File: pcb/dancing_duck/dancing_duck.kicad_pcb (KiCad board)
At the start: 2 copper layers, 60.2 x 53.6 mm, 12 parts, among them J1 Conn_01x02, J2 Conn_01x02, J3 Conn_01x02, J4 Conn_01x02, J5 Conn_01x02_Pin, J6 Conn_01x01_Pin

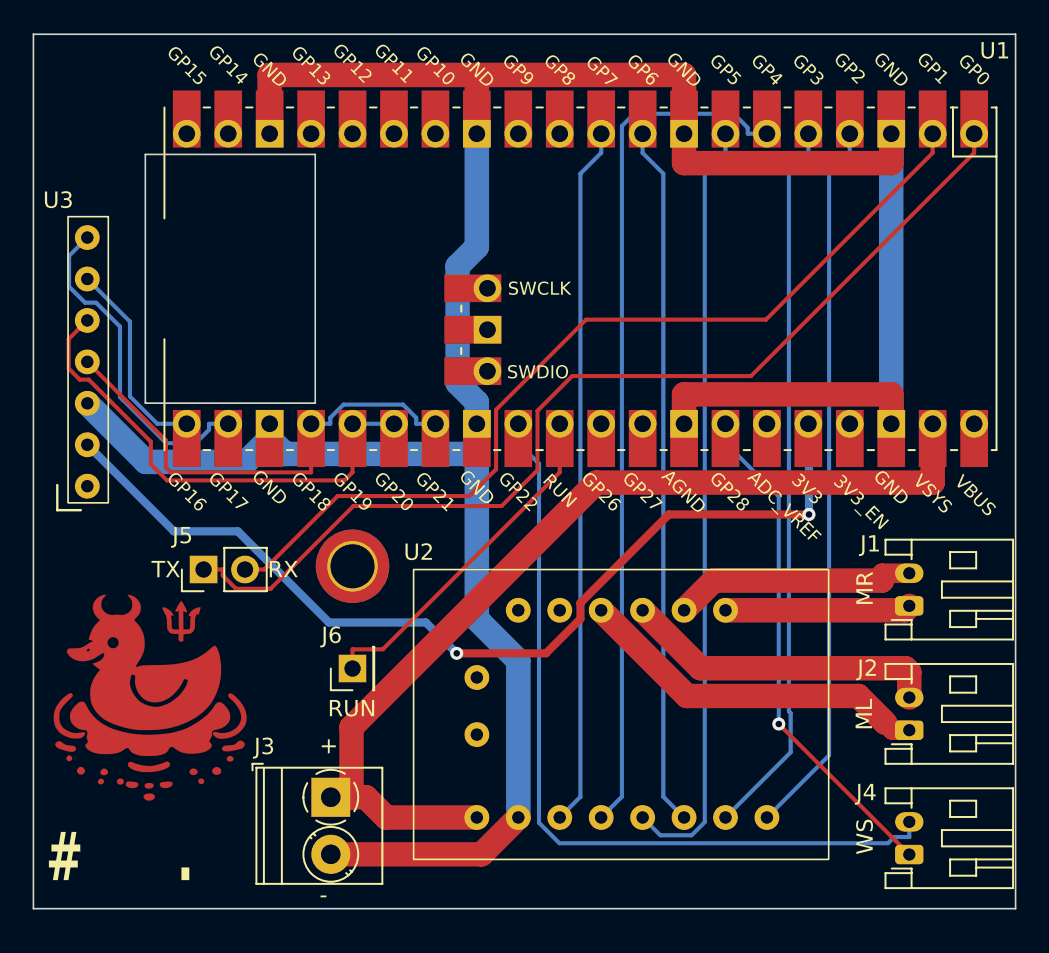
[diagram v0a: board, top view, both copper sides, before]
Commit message: feat: add battery adc to pcb
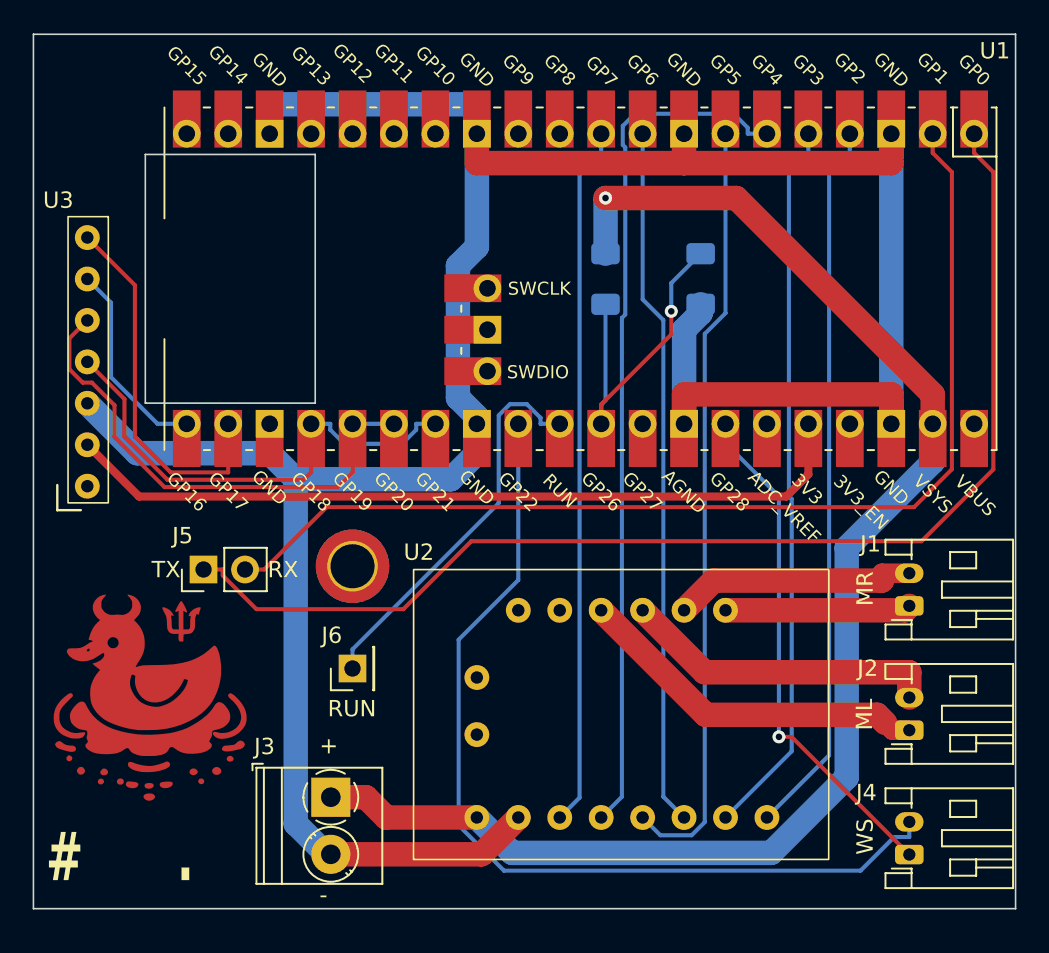
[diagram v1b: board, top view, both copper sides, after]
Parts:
- added R1: 220k, Resistor_SMD:R_1206_3216Metric_Pad1.30x1.75mm_HandSolder, B.Cu at (159.3, 85.3)
- added R2: 330k, Resistor_SMD:R_1206_3216Metric_Pad1.30x1.75mm_HandSolder, B.Cu at (165.1, 85.3)
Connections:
- U1 pad 31: unconnected-(U1-GP26-Pad31) -> Net-(U1-GP26)
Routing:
- net VCC: track 59.2 -> 89.1 mm, vias 0 -> 1
- net Net-(U1-GP26): track 0.00 -> 20.4 mm, vias 0 -> 1
- net Net-(J5-Pin_1): track 62.3 -> 74.2 mm
- net Net-(J5-Pin_2): track 56.0 -> 66.9 mm
- net +3V3: track 59.2 -> 49.2 mm, vias 2 -> 0
- net Net-(J4-Pin_2): track 49.3 -> 56.7 mm
- net GND: track 170.2 -> 174.2 mm
- net Net-(J6-Pin_1): track 21.3 -> 24.0 mm
- net Net-(U1-GP17): track 20.4 -> 23.0 mm
- net Net-(U1-GP18): track 29.5 -> 30.3 mm
- net Net-(U1-GP19): track 30.2 -> 30.8 mm

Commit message: fix: update pcb to beta
- Fix daughter board pin hole size
- Add better support for connecting J-Link
- Update silkscreen
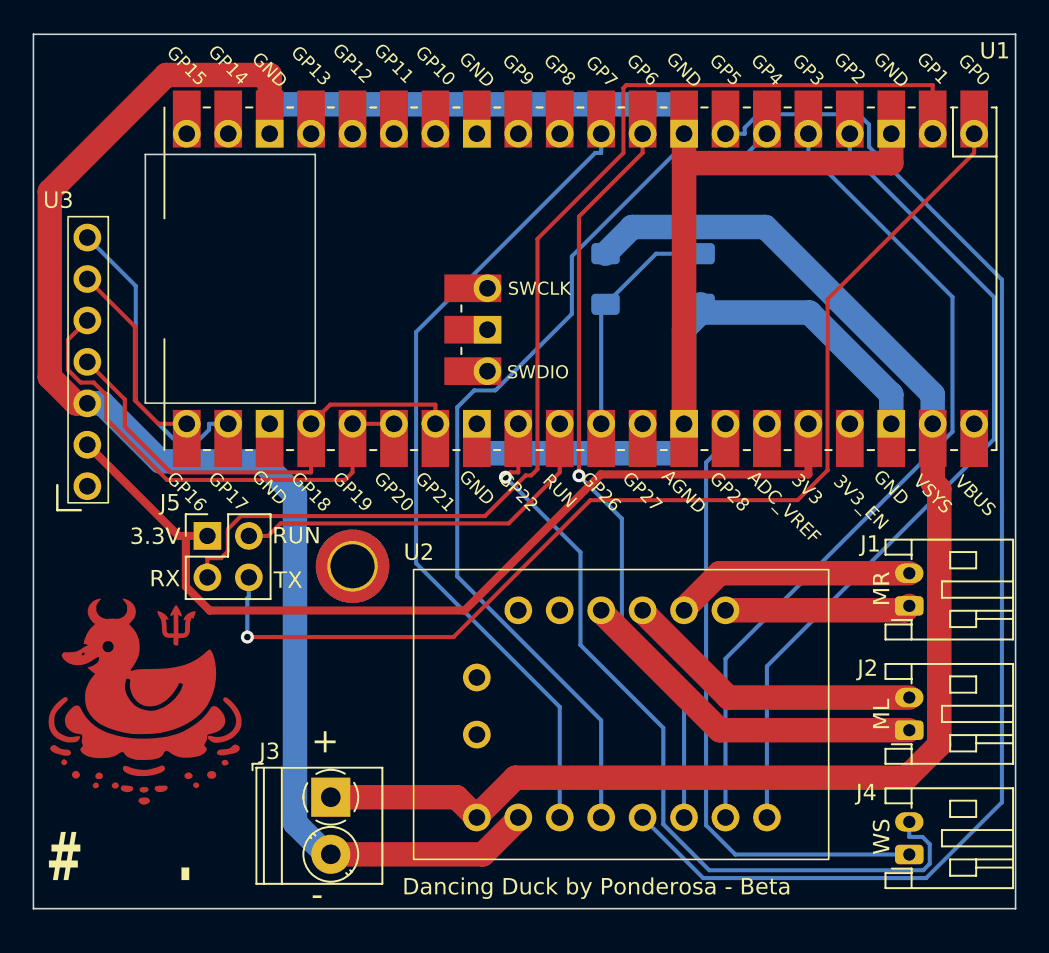
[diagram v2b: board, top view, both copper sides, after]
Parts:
- removed J6: Conn_01x01_Pin, Connector_PinHeader_2.54mm:PinHeader_1x01_P2.54mm_Vertical
- J5: value Conn_01x02_Pin -> Conn_02x02_Counter_Clockwise; footprint Connector_PinHeader_2.54mm:PinHeader_1x02_P2.54mm_Vertical -> Connector_PinHeader_2.54mm:PinHeader_2x02_P2.54mm_Vertical
- moved J5 2.07 mm to (134.9, 101.1), turned to 0 degrees
- moved G*** 0.39 mm to (131.1, 111.3)
- moved G_LOGO 0.39 mm to (131.1, 111.3)
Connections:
- J5 pad 1: Net-(J5-Pin_1) -> +3V3
- U1 pad 1: Net-(J5-Pin_1) -> Net-(J5-Pin_4)
- U1 pad 2: Net-(J5-Pin_2) -> Net-(J5-Pin_3)
- U1 pad 30: Net-(J6-Pin_1) -> Net-(J5-Pin_2)
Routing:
- net Net-(J5-Pin_1): track 74.2 -> 0.00 mm
- net Net-(J5-Pin_3): track 0.00 -> 72.0 mm
- net Net-(J5-Pin_4): track 0.00 -> 67.8 mm, vias 0 -> 1
- net Net-(J5-Pin_2): track 66.9 -> 23.6 mm
- net Net-(U1-GP5): track 47.3 -> 80.2 mm
- net Net-(J6-Pin_1): track 24.0 -> 0.00 mm
- net GND: track 174.2 -> 190.2 mm
- net +3V3: track 49.2 -> 58.1 mm
- net Net-(U1-GP7): track 43.0 -> 50.5 mm
- net Net-(U1-GP2): track 44.0 -> 51.3 mm
- net Net-(U1-GP3): track 44.2 -> 51.3 mm
- net Net-(J4-Pin_1): track 31.5 -> 38.3 mm, vias 1 -> 0
- net Net-(J4-Pin_2): track 56.7 -> 50.4 mm, vias 0 -> 1
- net Net-(U1-GP26): track 20.4 -> 14.6 mm, vias 1 -> 0
- net Net-(U1-GP17): track 23.0 -> 18.7 mm
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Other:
- board text added: "3.3V"
- board text added: "Dancing Duck by Ponderosa - Beta"
- board text added: "https://github.com/Ponderosa/dancing_duck"

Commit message: fix: add capacitor to pcb
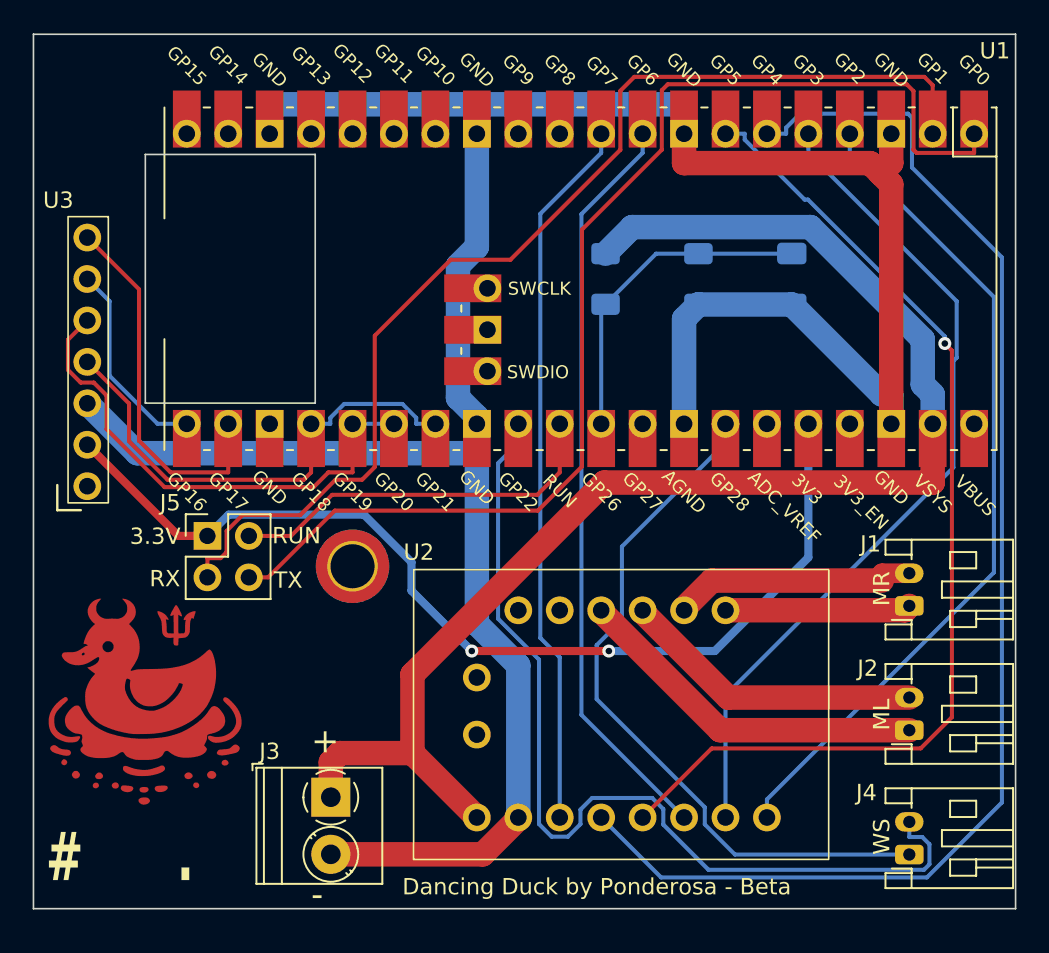
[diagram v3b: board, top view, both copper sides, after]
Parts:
- added C1: 1000pf, Capacitor_SMD:C_1206_3216Metric_Pad1.33x1.80mm_HandSolder, B.Cu at (170.7, 85.3)
- moved R2 0.14 mm to (165.0, 85.3)
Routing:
- net Net-(U1-GP4): track 56.8 -> 82.0 mm
- net GND: track 190.2 -> 170.2 mm
- net Net-(U1-GP5): track 80.2 -> 63.8 mm, vias 0 -> 1
- net Net-(J4-Pin_2): track 50.4 -> 57.9 mm, vias 1 -> 0
- net Net-(U1-GP7): track 50.5 -> 43.9 mm
- net Net-(U1-GP26): track 14.6 -> 20.1 mm
- net Net-(J4-Pin_1): track 38.3 -> 43.9 mm
- net Net-(J5-Pin_4): track 67.8 -> 72.6 mm, vias 1 -> 0
- net Net-(U1-GP17): track 18.7 -> 23.0 mm
- net +3V3: track 58.1 -> 62.1 mm, vias 0 -> 2
- net Net-(J5-Pin_3): track 72.0 -> 68.6 mm
- net Net-(U1-GP19): track 30.3 -> 31.0 mm
- net Net-(U1-GP18): track 29.8 -> 30.3 mm
- net Net-(U1-GP6): track 46.2 -> 46.1 mm, vias 1 -> 0

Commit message: feat: add RX to GND solder bridge to PCB
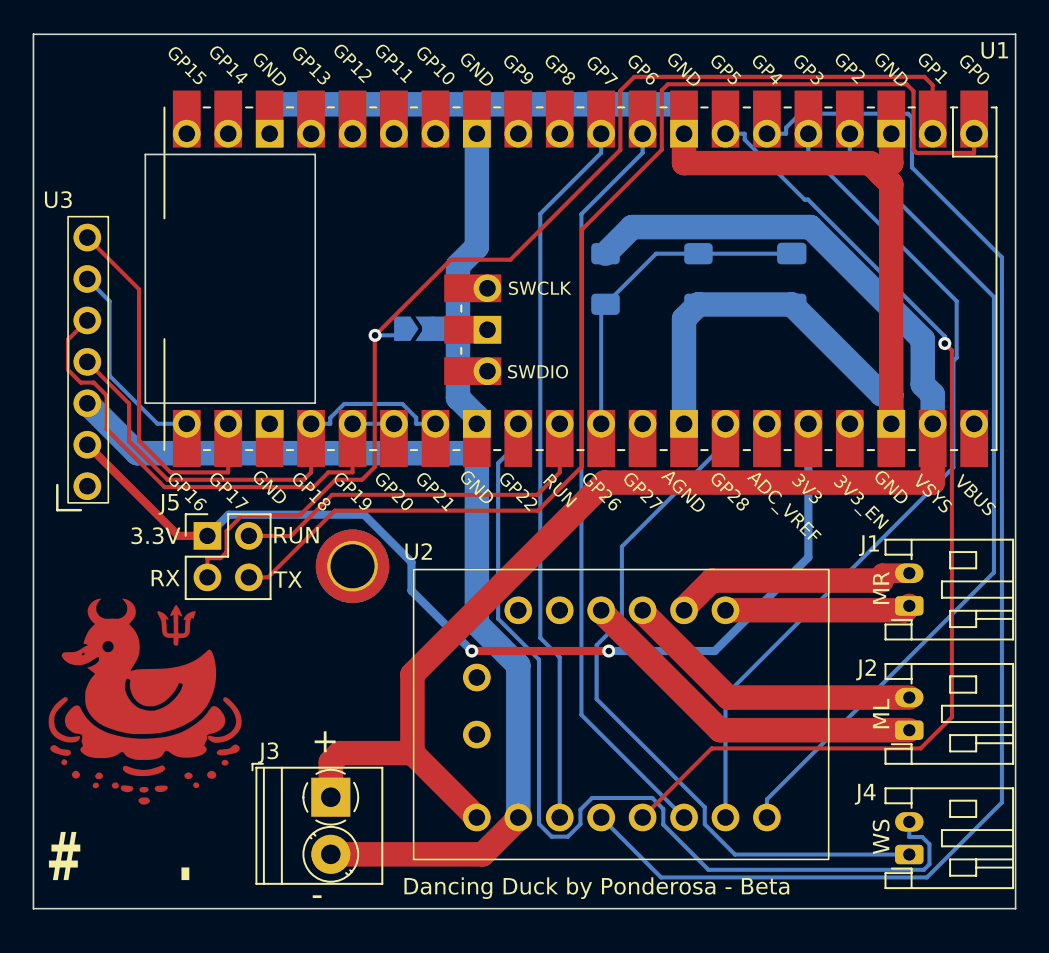
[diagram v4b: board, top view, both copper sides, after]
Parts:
- added R3: 0 DNP, Jumper:SolderJumper-2_P1.3mm_Open_TrianglePad1.0x1.5mm, B.Cu at (147.5, 88.4)
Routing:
- net Net-(J5-Pin_3): track 68.6 -> 70.5 mm, vias 0 -> 1
- net GND: track 170.2 -> 171.6 mm
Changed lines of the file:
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@@
     )
+  )
+  (footprint "Jumper:SolderJumper-2_P1.3mm_Open_TrianglePad1.0x1.5mm" (layer "B.Cu")
+    (at 147.537 88.392)
+    (descr "SMD Solder Jumper, 1x1.5mm Triangular Pads, 0.3mm gap, open")
+    (tags "solder jumper open")
+    (property "Sheetfile" "dancing_duck.kicad_sch")
+    (property "Sheetname" "")
+    (property "ki_description" "Resistor, US symbol")
+    (property "ki_keywords" "R res resistor")
+    (attr exclude_from_pos_files)
+    (fp_text reference "R3" (at 0 1.8) (layer "B.SilkS")
+        (effects (font (size 1 1) (thickness 0.15)) (justify mirror))
+    )
+    (fp_text value "0 DNP" (at 0 -1.9) (layer "B.Fab")
+        (effects (font (size 1 1) (thickness 0.15)) (justify mirror))
+    )
+    (fp_line (start -1.4 -1) (end -1.4 1)
+      (stroke (width 0.12) (type solid)) (layer "B.SilkS"))
+    (fp_line (start -1.4 1) (end 1.4 1)
+      (stroke (width 0.12) (type solid)) (layer "B.SilkS"))
+    (fp_line (start 1.4 -1) (end -1.4 -1)
+      (stroke (width 0.12) (type solid)) (layer "B.SilkS"))
+    (fp_line (start 1.4 1) (end 1.4 -1)
+      (stroke (width 0.12) (type solid)) (layer "B.SilkS"))
+    (fp_line (start -1.65 1.25) (end -1.65 -1.25)
+      (stroke (width 0.05) (type solid)) (layer "B.CrtYd"))
+    (fp_line (start -1.65 1.25) (end 1.65 1.25)
+      (stroke (width 0.05) (type solid)) (layer "B.CrtYd"))
+    (fp_line (start 1.65 -1.25) (end -1.65 -1.25)
+      (stroke (width 0.05) (type solid)) (layer "B.CrtYd"))
+    (fp_line (start 1.65 -1.25) (end 1.65 1.25)
+      (stroke (width 0.05) (type solid)) (layer "B.CrtYd"))
+    (pad "1" smd custom (at -0.725 0) (size 0.3 0.3) (layers "B.Cu" "B.Mask")
+      (net 42 "Net-(J5-Pin_3)") (pintype "passive") (zone_connect 2)
+      (options (clearance outline) (anchor rect))
+      (primitives
+        (gr_poly
+          (pts
+            (xy 1 0)
+            (xy 0.5 -0.75)
+            (xy -0.5 -0.75)
+            (xy -0.5 0.75)
+            (xy 0.5 0.75)
+          )
+          (width 0) (fill yes))
+      ))
+    (pad "2" smd custom (at 0.725 0) (size 0.3 0.3) (layers "B.Cu" "B.Mask")
+      (net 6 "GND") (pintype "passive") (zone_connect 2)
+      (options (clearance outline) (anchor rect))
+      (primitives
+        (gr_poly
+          (pts
+            (xy 0.5 -0.75)
+            (xy -0.65 -0.75)
+            (xy -0.15 0)
+            (xy -0.65 0.75)
+            (xy 0.5 0.75)
+          )
+          (width 0) (fill yes))
+      ))
   )
   (footprint "Resistor_SMD:R_1206_3216Metric_Pad1.30x1.75mm_HandSolder" (layer "B.Cu")
@@
   (segment (start 176.1996 92.4181) (end 170.688 86.9065) (width 1.5) (layer "B.Cu") (net 6))
   (segment (start 151.384 74.6396) (end 151.3825 74.6381) (width 1.5) (layer "B.Cu") (net 6))
+  (segment (start 150.2257 88.392) (end 148.762 88.392) (width 1.5) (layer "B.Cu") (net 6))
+  (segment (start 150.2257 84.5324) (end 150.2257 88.392) (width 1.5) (layer "B.Cu") (net 6))
   (segment (start 164.964 86.894) (end 164.964 86.9065) (width 1.5) (layer "B.Cu") (net 6))
   (segment (start 176.784 92.4181) (end 176.1996 92.4181) (width 1.5) (layer "B.Cu") (net 6))
-  (segment (start 150.2257 84.5324) (end 150.2257 92.6262) (width 1.5) (layer "B.Cu") (net 6))
+  (segment (start 150.2257 88.392) (end 150.2257 92.6262) (width 1.5) (layer "B.Cu") (net 6))
   (segment (start 138.6855 96.0219) (end 138.684 96.0204) (width 1.5) (layer "B.Cu") (net 6))
   (segment (start 151.384 83.3741) (end 150.2257 84.5324) (width 1.5) (layer "B.Cu") (net 6))
@@
   (segment (start 159.27 86.894) (end 159.004 87.16) (width 0.25) (layer "B.Cu") (net 29))
   (segment (start 164.964 83.794) (end 162.37 83.794) (width 0.25) (layer "B.Cu") (net 29))
-  (segment (start 144.3491 97.6488) (end 145.1271 96.8708) (width 0.25) (layer "F.Cu") (net 42))
-  (segment (start 140.5441 99.8221) (end 142.7174 97.6488) (width 0.25) (layer "F.Cu") (net 42))
-  (segment (start 137.012 99.8221) (end 140.5441 99.8221) (width 0.25) (layer "F.Cu") (net 42))
-  (segment (start 145.1271 88.8178) (end 149.7796 84.1653) (width 0.25) (layer "F.Cu") (net 42))
-  (segment (start 135.6782 102.4551) (end 136.0459 102.0874) (width 0.25) (layer "F.Cu") (net 42))
+  (segment (start 140.5441 99.8221) (end 137.012 99.8221) (width 0.25) (layer "F.Cu") (net 42))
+  (segment (start 161.0347 72.9535) (end 178.8144 72.9535) (width 0.25) (layer "F.Cu") (net 42))
+  (segment (start 179.324 73.4631) (end 179.324 76.44) (width 0.25) (layer "F.Cu") (net 42))
   (segment (start 153.441 84.1653) (end 160.1809 77.4254) (width 0.25) (layer "F.Cu") (net 42))
-  (segment (start 145.1271 96.8708) (end 145.1271 88.8178) (width 0.25) (layer "F.Cu") (net 42))
+  (segment (start 145.1271 88.8178) (end 145.1271 96.8708) (width 0.25) (layer "F.Cu") (net 42))
+  (segment (start 160.1809 77.4254) (end 160.1809 73.8073) (width 0.25) (layer "F.Cu") (net 42))
+  (segment (start 136.0459 100.7882) (end 136.0459 102.0874) (width 0.25) (layer "F.Cu") (net 42))
+  (segment (start 145.1271 96.8708) (end 144.3491 97.6488) (width 0.25) (layer "F.Cu") (net 42))
+  (segment (start 142.7174 97.6488) (end 140.5441 99.8221) (width 0.25) (layer "F.Cu") (net 42))
+  (segment (start 145.195181 88.775695) (end 145.169205 88.775695) (width 0.25) (layer "F.Cu") (net 42))
+  (segment (start 144.3491 97.6488) (end 142.7174 97.6488) (width 0.25) (layer "F.Cu") (net 42))
+  (segment (start 178.8144 72.9535) (end 179.324 73.4631) (width 0.25) (layer "F.Cu") (net 42))
+  (segment (start 134.869 102.4551) (end 134.869 103.632) (width 0.25) (layer "F.Cu") (net 42))
+  (segment (start 135.6782 102.4551) (end 134.869 102.4551) (width 0.25) (layer "F.Cu") (net 42))
   (segment (start 160.1809 73.8073) (end 161.0347 72.9535) (width 0.25) (layer "F.Cu") (net 42))
-  (segment (start 142.7174 97.6488) (end 144.3491 97.6488) (width 0.25) (layer "F.Cu") (net 42))
-  (segment (start 161.0347 72.9535) (end 178.8144 72.9535) (width 0.25) (layer "F.Cu") (net 42))
+  (segment (start 145.195181 88.775695) (end 145.195181 88.749719) (width 0.25) (layer "F.Cu") (net 42))
+  (segment (start 136.0459 102.0874) (end 135.6782 102.4551) (width 0.25) (layer "F.Cu") (net 42))
+  (segment (start 145.195181 88.749719) (end 149.7796 84.1653) (width 0.25) (layer "F.Cu") (net 42))
   (segment (start 149.7796 84.1653) (end 153.441 84.1653) (width 0.25) (layer "F.Cu") (net 42))
-  (segment (start 134.869 103.632) (end 134.869 102.4551) (width 0.25) (layer "F.Cu") (net 42))
-  (segment (start 179.324 76.44) (end 179.324 73.4631) (width 0.25) (layer "F.Cu") (net 42))
-  (segment (start 160.1809 77.4254) (end 160.1809 73.8073) (width 0.25) (layer "F.Cu") (net 42))
-  (segment (start 136.0459 102.0874) (end 136.0459 100.7882) (width 0.25) (layer "F.Cu") (net 42))
-  (segment (start 136.0459 100.7882) (end 137.012 99.8221) (width 0.25) (layer "F.Cu") (net 42))
-  (segment (start 178.8144 72.9535) (end 179.324 73.4631) (width 0.25) (layer "F.Cu") (net 42))
-  (segment (start 134.869 102.4551) (end 135.6782 102.4551) (width 0.25) (layer "F.Cu") (net 42))
+  (segment (start 145.169205 88.775695) (end 145.1271 88.8178) (width 0.25) (layer "F.Cu") (net 42))
+  (segment (start 137.012 99.8221) (end 136.0459 100.7882) (width 0.25) (layer "F.Cu") (net 42))
+  (via (at 145.14754 88.798071) (size 0.8) (drill 0.4) (layers "F.Cu" "B.Cu") (net 42))
+  (segment (start 145.14754 88.798071) (end 146.405929 88.798071) (width 0.25) (layer "B.Cu") (net 42))
+  (segment (start 146.405929 88.798071) (end 146.812 88.392) (width 0.25) (layer "B.Cu") (net 42))
   (segment (start 157.8271 96.8377) (end 157.8271 82.3192) (width 0.25) (layer "F.Cu") (net 43))
   (segment (start 178.3386 77.6169) (end 181.864 77.6169) (width 0.25) (layer "F.Cu") (net 43))
